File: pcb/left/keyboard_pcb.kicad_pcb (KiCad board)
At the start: 2 copper layers, 138.8 x 89.9 mm, 106 parts, among them J1 TRRS, J2 Alt. Battery, J3 Alt. Switch, K00 KEYSW, K01 KEYSW, K02 KEYSW, K03 KEYSW, K04 KEYSW, K05 KEYSW, K10 KEYSW, K11 KEYSW, K12 KEYSW, K13 KEYSW, K14 KEYSW, K15 KEYSW, K20 KEYSW, K21 KEYSW, K22 KEYSW, K23 KEYSW, K24 KEYSW, K25 KEYSW, K33 KEYSW, K34 KEYSW, K35 KEYSW, U1 Flippable RP2040 ProMicro/nic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

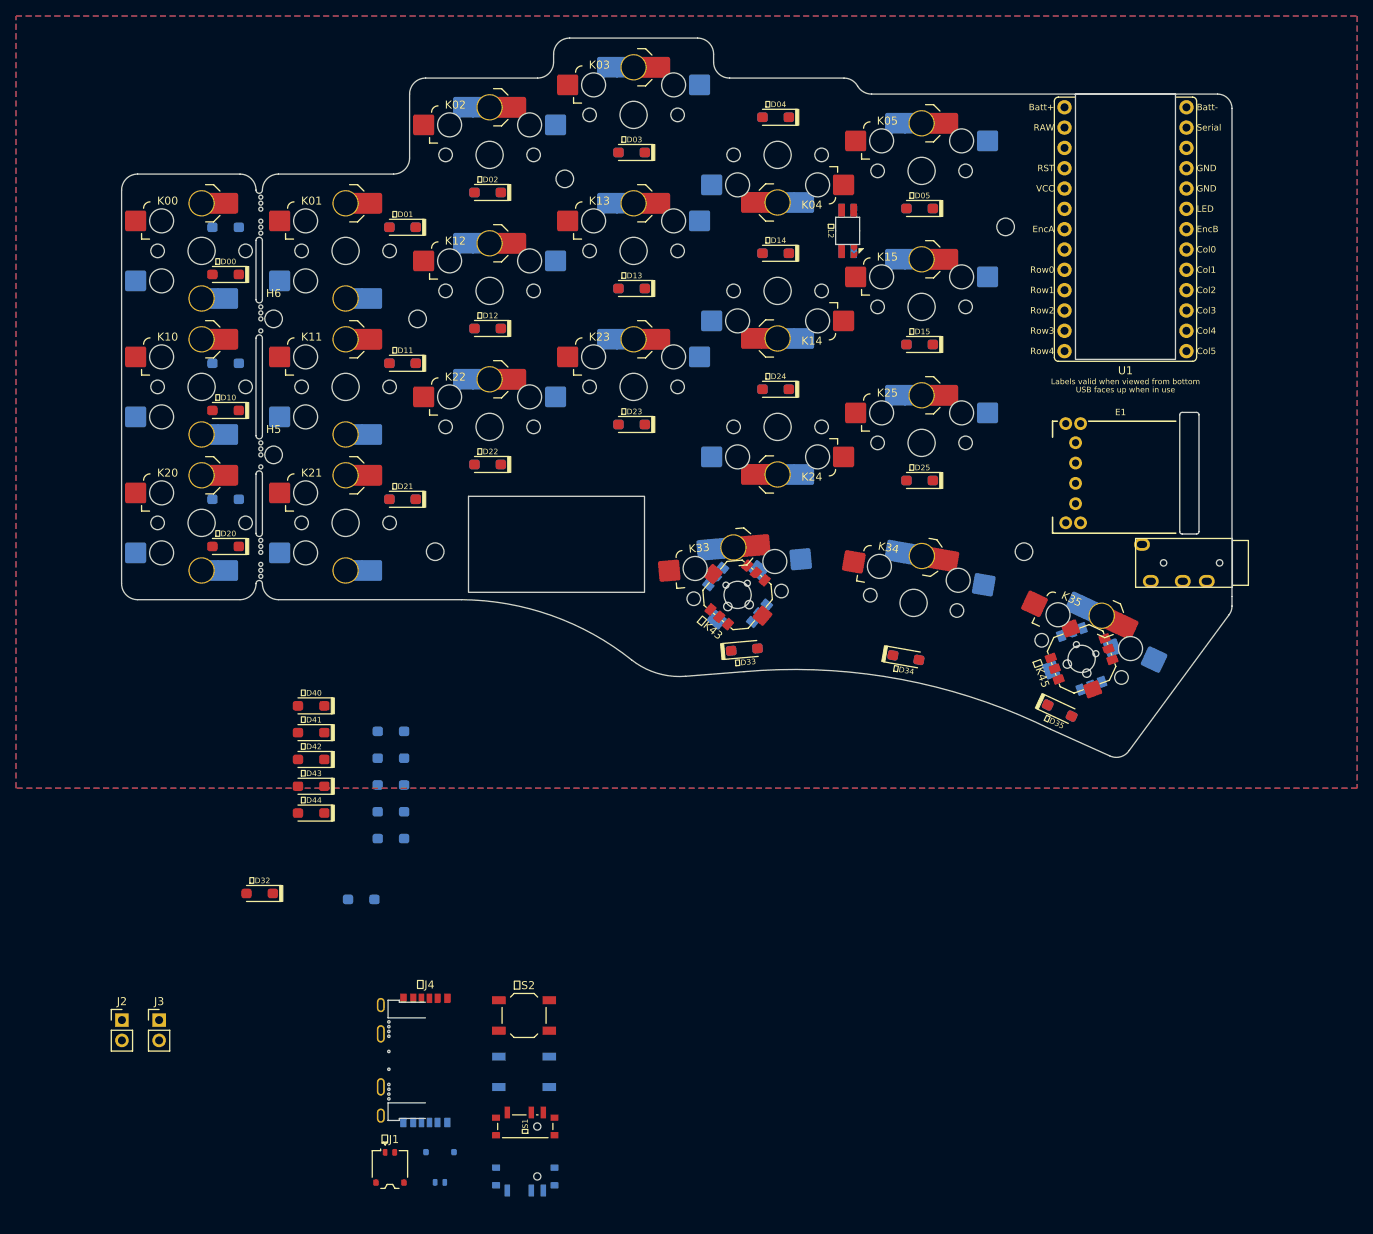
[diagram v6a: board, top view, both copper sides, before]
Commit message: Rough layout of all components, split switch jumper into two jumpers
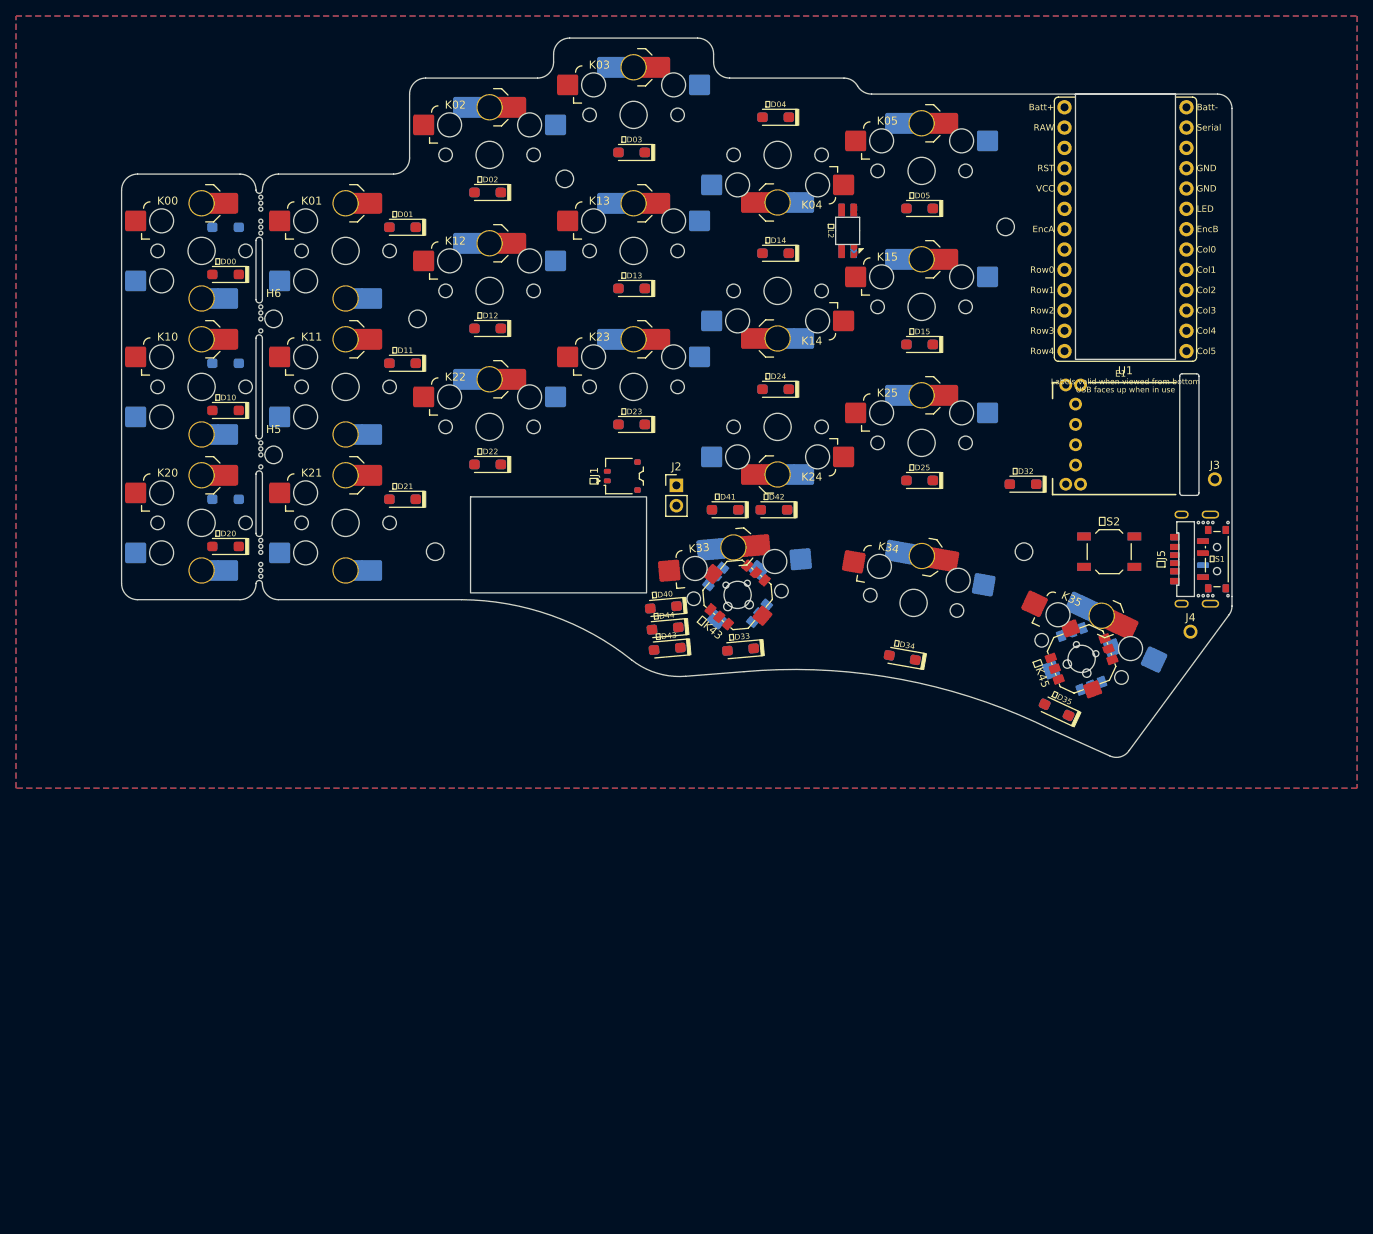
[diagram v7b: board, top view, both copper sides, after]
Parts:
- removed J1: TRRS, Keebio-Parts:TRRS-PJ-320A
- added J4: Conn_01x01_Socket, beekeeb_lib:SinglePad, F.Cu at (197.6, 117.6)
- J3: value Alt. Switch -> Conn_01x01_Socket; footprint Connector_PinHeader_2.54mm:PinHeader_1x02_P2.54mm_Vertical -> beekeeb_lib:SinglePad
- moved J3 148.3 mm to (200.7, 98.6)
- moved 左J5 118.2 mm to (200.1, 108.5), turned to -90 degrees
- moved 左S1 115.9 mm to (200.6, 108.5), turned to -90 degrees
- moved 右J5 114.7 mm to (200.1, 108.5), turned to 90 degrees
- moved 右S1 111.4 mm to (200.6, 108.5), turned to 90 degrees
- moved 右D32 108.3 mm to (176.7, 99.2)
- moved 左S2 97.9 mm to (187.5, 107.6)
- moved 左D32 97.7 mm to (176.7, 99.2), turned to 180 degrees
- moved J2 96.3 mm to (133.3, 99.3)
- moved 右S2 93.3 mm to (187.5, 107.6)
- moved 右J1 91.2 mm to (126.6, 98.2), turned to 90 degrees
- moved 左J1 89.4 mm to (126.6, 98.2), turned to -90 degrees
- moved 右D42 65.7 mm to (145.5, 102.4)
- moved 左D42 59.0 mm to (145.5, 102.4)
- moved 右D41 58.8 mm to (139.4, 102.4)
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- renumbered 右J4 to 右J5, 左J4 to 左J5

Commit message: Add outlines of Piantor and Piantor Pro cases and align USB ports as needed
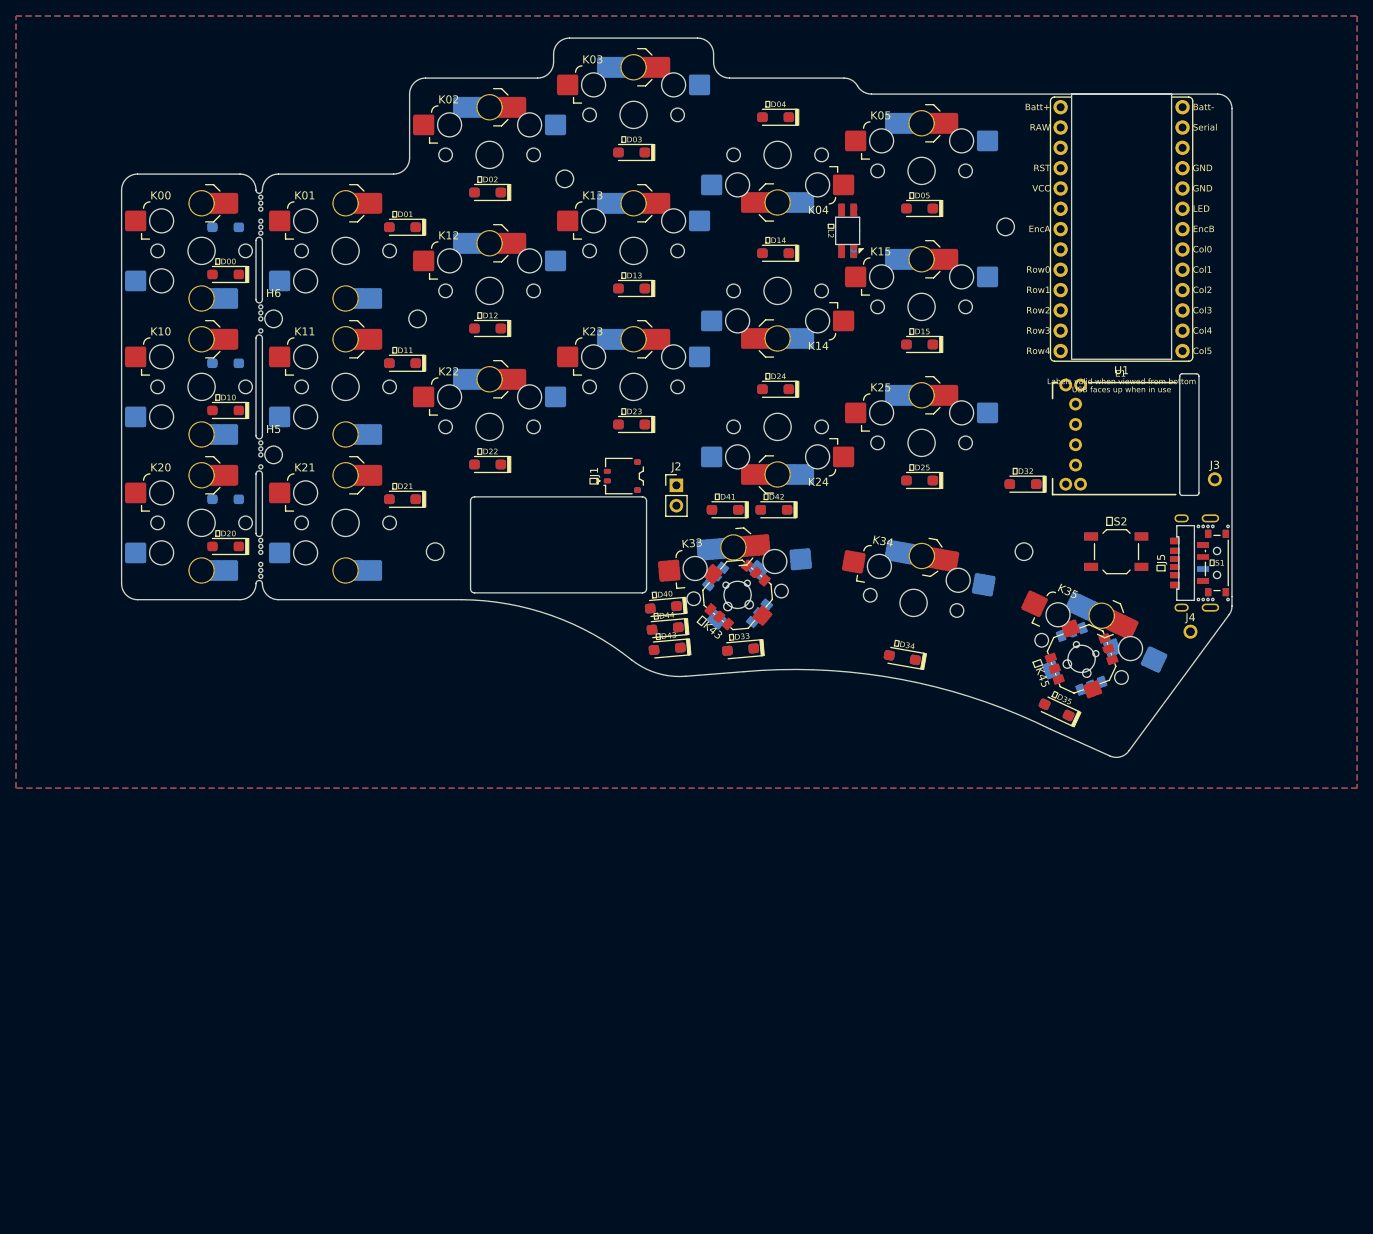
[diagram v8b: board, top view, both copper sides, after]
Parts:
- moved 右S2 0.91 mm to (188.4, 107.6)
- moved 左S2 0.86 mm to (188.3, 107.6)
- moved U1 0.48 mm to (189.0, 68.5)
- moved 右J5 0.48 mm to (200.1, 109.0)
- moved 右S1 0.48 mm to (200.6, 109.0)
- moved 左J5 0.48 mm to (200.1, 109.0)
- moved 左S1 0.48 mm to (200.6, 109.0)
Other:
- board text added: "Piantor Case"
- board text added: "Piantor Pro Case"
